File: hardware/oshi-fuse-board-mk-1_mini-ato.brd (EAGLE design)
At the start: 22 x 17 mm, 7 parts

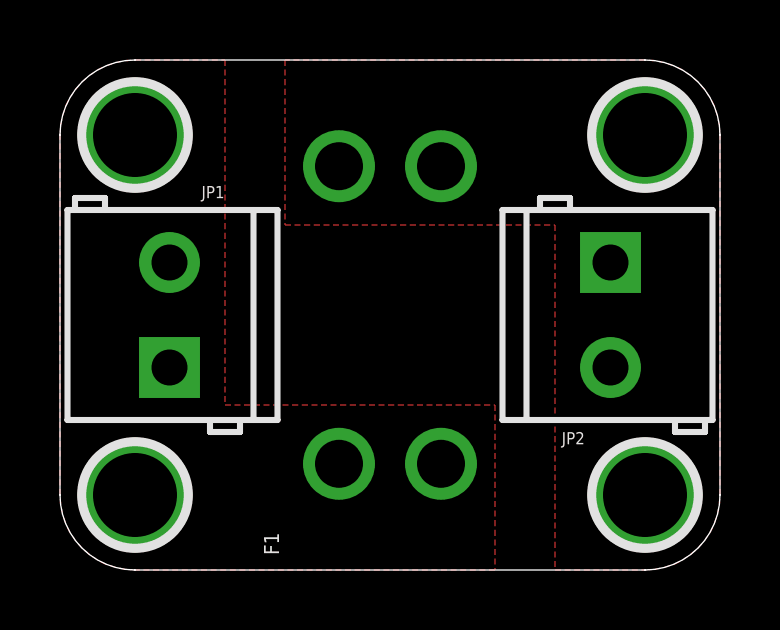
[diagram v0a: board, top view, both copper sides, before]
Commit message: finished layout for the miniato version
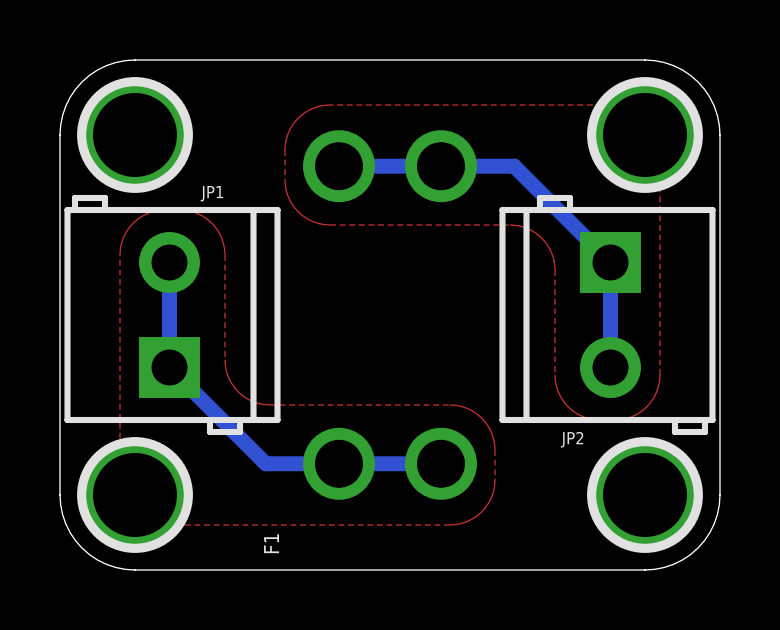
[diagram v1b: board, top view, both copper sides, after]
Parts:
- added U$1: (no value), A_butts:COW_SMALL
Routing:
- net B: track 0.00 -> 13.9 mm
- net A: track 0.00 -> 13.9 mm
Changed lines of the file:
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@@
 <layer number="27" name="tValues" color="7" fill="1" visible="yes" active="yes"/>
 <layer number="28" name="bValues" color="7" fill="1" visible="yes" active="yes"/>
-<layer number="29" name="tStop" color="7" fill="3" visible="no" active="yes"/>
-<layer number="30" name="bStop" color="7" fill="6" visible="no" active="yes"/>
+<layer number="29" name="tStop" color="7" fill="3" visible="yes" active="yes"/>
+<layer number="30" name="bStop" color="7" fill="6" visible="yes" active="yes"/>
 <layer number="31" name="tCream" color="7" fill="4" visible="no" active="yes"/>
 <layer number="32" name="bCream" color="7" fill="5" visible="no" active="yes"/>
@@
 <wire x1="19.5" y1="17" x2="2.5" y2="17" width="0" layer="20"/>
 <wire x1="2.5" y1="17" x2="0" y2="14.5" width="0" layer="20" curve="90"/>
-<text x="15" y="8.5" size="0.8" layer="22" font="vector" ratio="12" rot="MR90" align="bottom-center">"OHSI-" FUSE HOLDER</text>
+<text x="15.5" y="8.5" size="0.8" layer="22" font="vector" ratio="12" rot="MR90" align="bottom-center">"OHSI-" FUSE HOLDER</text>
 <text x="6.5" y="13" size="0.5" layer="22" font="vector" ratio="12" rot="MR90" align="bottom-center">Rev 1.0</text>
-<text x="7" y="4" size="0.5" layer="22" font="vector" ratio="12" rot="MR270" align="bottom-center">by schizobovine
+<text x="7.5" y="4" size="0.5" layer="22" font="vector" ratio="12" rot="MR270" align="bottom-center">by schizobovine
 &lt;sean@yak.net&gt;</text>
-<text x="5.5" y="13" size="0.5" layer="22" font="vector" ratio="12" rot="MR90" align="bottom-center">CC-4.0-BY-SA</text>
-<text x="14" y="8.5" size="0.5" layer="22" font="vector" ratio="12" rot="MR90" align="bottom-center">MINI-ATO</text>
+<text x="5.5" y="4" size="0.5" layer="22" font="vector" ratio="12" rot="MR90" align="bottom-center">CC-4.0-BY-SA</text>
+<text x="5.5" y="13" size="0.5" layer="22" font="vector" ratio="12" rot="MR90" align="bottom-center">MINI-ATO</text>
 </plain>
 <attributes>
@@
 <element name="H3" library="A_butts" package="HOLE-#2" value="HOLE#2" x="19.5" y="2.5"/>
 <element name="H4" library="A_butts" package="HOLE-#2" value="HOLE#2" x="2.5" y="2.5"/>
+<element name="U$1" library="A_butts" package="COW_SMALL" value="" x="12" y="8.5" rot="MR90"/>
 </elements>
 <signals>
 <signal name="A">
+<polygon width="0.1524" layer="1">
+<vertex x="14.5" y="4"/>
+<vertex x="14.5" y="3" curve="-90"/>
+<vertex x="13" y="1.5"/>
+<vertex x="2" y="1.5"/>
+<vertex x="2" y="10.5" curve="-90"/>
+<vertex x="3.5" y="12"/>
+<vertex x="4" y="12" curve="-90"/>
+<vertex x="5.5" y="10.5"/>
+<vertex x="5.5" y="7" curve="90"/>
+<vertex x="7" y="5.5"/>
+<vertex x="13" y="5.5" curve="-90"/>
+</polygon>
 <contactref element="JP1" pad="1"/>
+<contactref element="JP1" pad="2"/>
+<contactref element="F1" pad="P1@2"/>
 <contactref element="F1" pad="P1@1"/>
-<contactref element="F1" pad="P1@2"/>
-<contactref element="JP1" pad="2"/>
-<polygon width="0.1524" layer="1">
-<vertex x="14.5" y="0"/>
-<vertex x="2.5" y="0" curve="-90"/>
-<vertex x="0" y="2.5"/>
-<vertex x="0" y="14.5" curve="-90"/>
-<vertex x="2.5" y="17"/>
-<vertex x="5.5" y="17"/>
-<vertex x="5.5" y="5.5"/>
-<vertex x="14.5" y="5.5"/>
-</polygon>
+<wire x1="3.65" y1="10.25" x2="3.65" y2="6.75" width="0.5" layer="16"/>
+<wire x1="3.65" y1="6.75" x2="6.86" y2="3.54" width="0.5" layer="16"/>
+<wire x1="6.86" y1="3.54" x2="9" y2="3.54" width="0.5" layer="16"/>
+<wire x1="9.3" y1="3.54" x2="12.7" y2="3.54" width="0.5" layer="16"/>
+<wire x1="9.3" y1="3.54" x2="9" y2="3.54" width="0.5" layer="16"/>
 </signal>
 <signal name="B">
+<polygon width="0.1524" layer="1">
+<vertex x="20" y="15.5"/>
+<vertex x="9" y="15.5" curve="90"/>
+<vertex x="7.5" y="14"/>
+<vertex x="7.5" y="13" curve="90"/>
+<vertex x="9" y="11.5"/>
+<vertex x="15" y="11.5" curve="-90"/>
+<vertex x="16.5" y="10"/>
+<vertex x="16.5" y="6.5" curve="90"/>
+<vertex x="18" y="5"/>
+<vertex x="18.5" y="5" curve="90"/>
+<vertex x="20" y="6.5"/>
+</polygon>
 <contactref element="F1" pad="P2@1"/>
+<contactref element="F1" pad="P2@2"/>
 <contactref element="JP2" pad="1"/>
 <contactref element="JP2" pad="2"/>
-<polygon width="0.1524" layer="1">
-<vertex x="7.5" y="17"/>
-<vertex x="7.5" y="11.5"/>
-<vertex x="16.5" y="11.5"/>
-<vertex x="16.5" y="0"/>
-<vertex x="19.5" y="0" curve="90"/>
-<vertex x="22" y="2.5"/>
-<vertex x="22" y="14.5" curve="90"/>
-<vertex x="19.5" y="17"/>
-</polygon>
-<contactref element="F1" pad="P2@2"/>
+<wire x1="9.3" y1="13.46" x2="12.7" y2="13.46" width="0.5" layer="16"/>
+<wire x1="18.35" y1="6.75" x2="18.35" y2="10.25" width="0.5" layer="16"/>
+<wire x1="12.7" y1="13.46" x2="15.14" y2="13.46" width="0.5" layer="16"/>
+<wire x1="15.14" y1="13.46" x2="18.35" y2="10.25" width="0.5" layer="16"/>
 </signal>
 </signals>
